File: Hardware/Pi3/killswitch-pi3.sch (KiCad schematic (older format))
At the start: 29 parts, among them J1 PWR_IN, J2 REMOTE, J3 PI, Q1 Q_PMOS_GSD, SW1 SW_Push, U1 ATTINY84-20SSU, U2 TSDP341xx, U3 AZ1117-3.3, U4 TXB0108DQSR

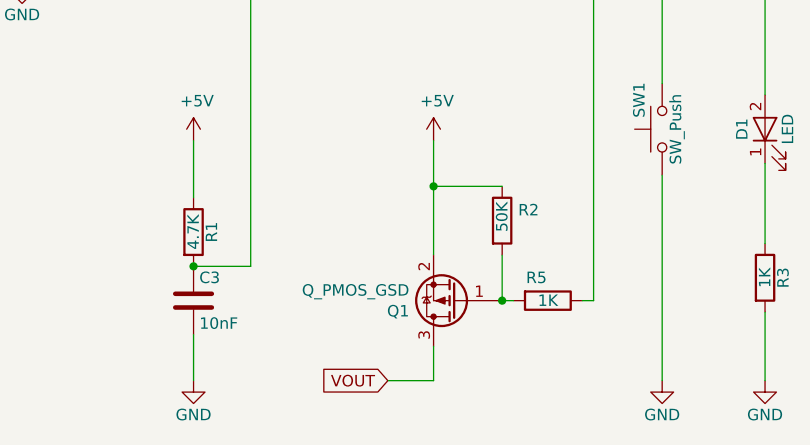
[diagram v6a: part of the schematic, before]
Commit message: added diode to backpower the killswitch from the pi (for programming)
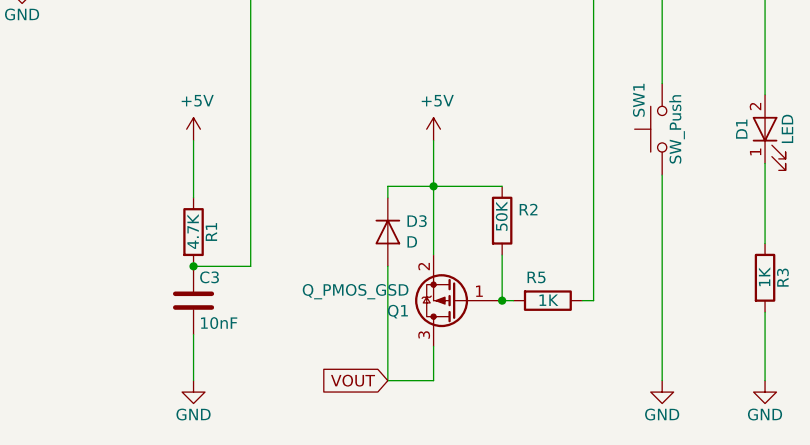
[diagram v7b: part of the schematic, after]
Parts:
- added D3: D, Diodes_SMD:D_0603, symbol device:D
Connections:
- net +5V: now also D3.1 (K)
- net VOUT: now also D3.2 (A)
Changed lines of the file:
@@
 Wire Wire Line
 	1850 1900 1850 1800
+$Comp
+L device:D D3
+U 1 1 5CA44E20
+P 3100 4550
+F 0 "D3" V 3054 4629 50  0000 L CNN
+F 1 "D" V 3145 4629 50  0000 L CNN
+F 2 "Diodes_SMD:D_0603" H 3100 4550 50  0001 C CNN
+F 3 "" H 3100 4550 50  0001 C CNN
+	1    3100 4550
+	0    1    1    0
+$EndComp
+Wire Wire Line
+	3100 4700 3100 5200
+Wire Wire Line
+	3100 4400 3100 4350
+Wire Wire Line
+	3100 4350 3300 4350
 $EndSCHEMATC
